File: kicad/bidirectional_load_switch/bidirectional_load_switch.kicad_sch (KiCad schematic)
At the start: 28 parts, among them J101 1017503, J102 Conn_01x09_Socket, J103 Conn_01x02_Socket, J104 Conn_01x02_Socket, J105 Conn_01x02_Socket, J106 Conn_01x02_Socket, J107 AVR-ISP-6, SW101 PTS526 SK15 SMTR2 LFS, U101 TMCS1101A3BQDR, U102 TLV75733PDBVR, U104 ATTINY85-20SU

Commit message: almost
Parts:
- added D101: CUS10S30_H3F, diode_CUS10S30_H3F:USC_TOS, symbol diode_CUS10S30_H3F:CUS10S30_H3F
- U102: footprint DBV0005A_N -> ldo_TLV75733PDBVR:DBV0005A_L
- renumbered C105 to C101, C106 to C102, C101 to C103, C107 to C104, C108 to C105, C104 to C106, C109 to C107, J103 to J102, J102 to J103, U104 to U103
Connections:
- net 3V3: now also D101.2
- net 5V: now also D101.1
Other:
- note added: "Power flags for DRC/ERC"
- moved on the sheet: C101, C102, C104, C105, J102, U102

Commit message: needs review
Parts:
- R101: value 10k -> 150
- SW101: footprint switch_switch_PTS526_SK15_SMTR2_LFS:SMT_FS -> switch_PTS526_SK15_SMTR2_LFS:SMT_FS
- U101: value TMCS1101A3BQDR -> TMCS1101A3BQDRQ1
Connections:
- net AC_in: now also U101.1 (IN+), U101.2 (IN+); no longer U101.3 (IN-), U101.4 (IN-)
- net AC_post_sense: now also U101.3 (IN-), U101.4 (IN-); no longer U101.1 (IN+), U101.2 (IN+)

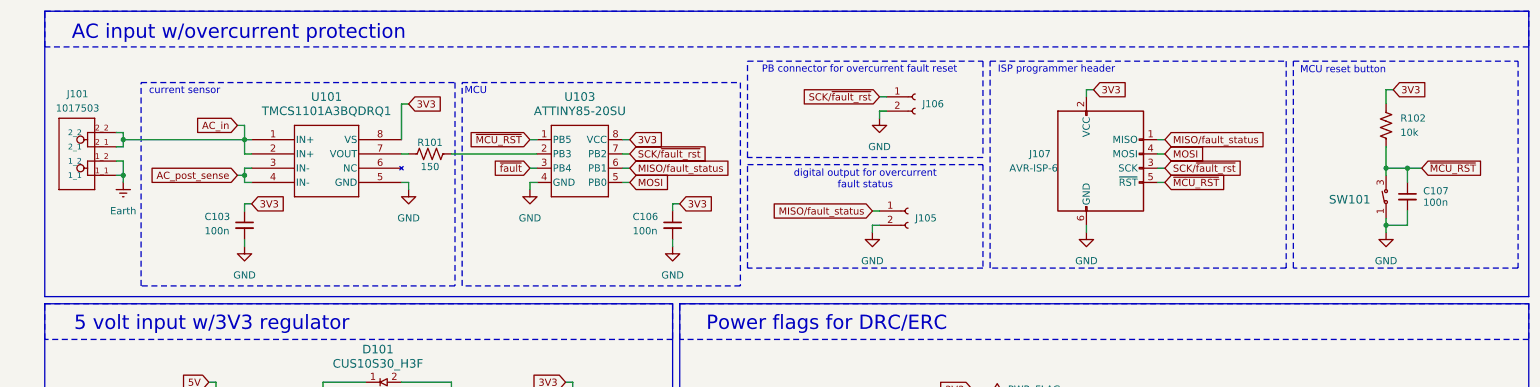
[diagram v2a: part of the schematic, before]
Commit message: added series diode for ISP 3V3 rail
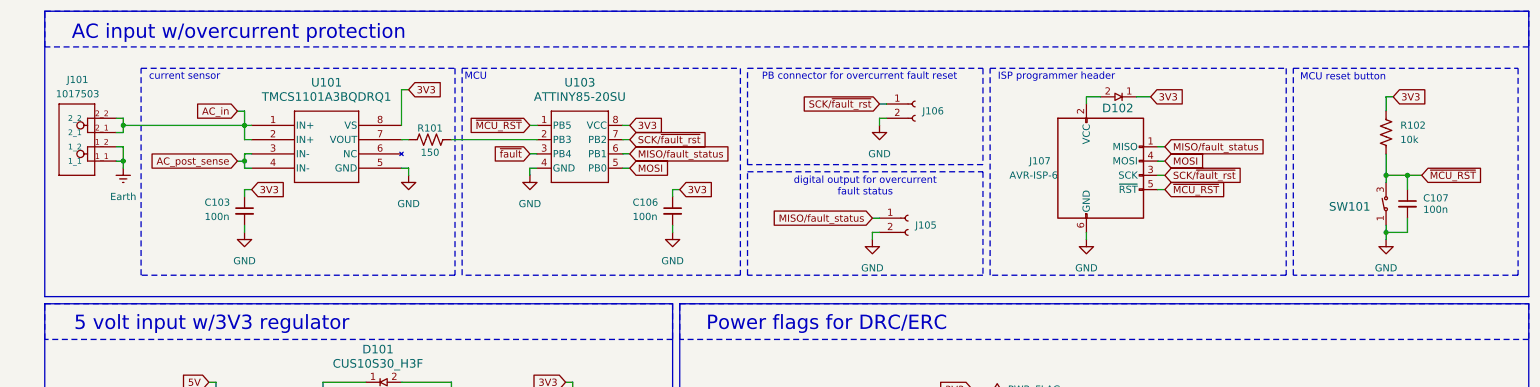
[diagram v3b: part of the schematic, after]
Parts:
- added D102: CUS10S30_H3F, diode_CUS10S30_H3F:USC_TOS, symbol diode_CUS10S30_H3F:CUS10S30_H3F
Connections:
- net 3V3: now also D102.1; no longer J107.2 (VCC)
- new net: D102.2, J107.2 (VCC)
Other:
- moved on the sheet: C103, C106, C107, J101, J105, J106, J107, R101, R102, SW101, U101, U103

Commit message: ready for order
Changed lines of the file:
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@@
 	(wire
 		(pts
-			(xy 110.49 92.71) (xy 110.49 93.98)
+			(xy 110.49 92.71) (xy 110.49 96.52)
 		)
 		(stroke
@@
 	(wire
 		(pts
-			(xy 46.99 92.71) (xy 46.99 93.98)
+			(xy 46.99 92.71) (xy 46.99 96.52)
 		)
 		(stroke
@@
 	(wire
 		(pts
-			(xy 128.27 54.61) (xy 128.27 55.88)
+			(xy 128.27 54.61) (xy 128.27 57.15)
 		)
 		(stroke
@@
 	(wire
 		(pts
-			(xy 52.07 54.61) (xy 52.07 55.88)
+			(xy 52.07 54.61) (xy 52.07 57.15)
 		)
 		(stroke
@@
 	(wire
 		(pts
-			(xy 25.4 92.71) (xy 25.4 90.17)
+			(xy 25.4 96.52) (xy 25.4 90.17)
 		)
 		(stroke
@@
 	(symbol
 		(lib_id "power:GND")
-		(at 128.27 55.88 0)
+		(at 128.27 57.15 0)
 		(unit 1)
 		(exclude_from_sim no)
@@
 		(fields_autoplaced yes)
 		(property "Reference" "#PWR0111"
-			(at 128.27 62.23 0)
+			(at 128.27 63.5 0)
 			(effects
 				(font
@@
 		)
 		(property "Value" "GND"
-			(at 128.27 60.96 0)
+			(at 128.27 62.23 0)
 			(effects
 				(font
@@
 		)
 		(property "Footprint" ""
-			(at 128.27 55.88 0)
+			(at 128.27 57.15 0)
 			(effects
 				(font
@@
 		)
 		(property "Datasheet" ""
-			(at 128.27 55.88 0)
+			(at 128.27 57.15 0)
 			(effects
 				(font
@@
 		)
 		(property "Description" "Power symbol creates a global label with name \"GND\" , ground"
-			(at 128.27 55.88 0)
+			(at 128.27 57.15 0)
 			(effects
 				(font
@@
 	(symbol
 		(lib_id "power:GND")
-		(at 25.4 92.71 0)
+		(at 25.4 96.52 0)
 		(unit 1)
 		(exclude_from_sim no)
@@
 		(fields_autoplaced yes)
 		(property "Reference" "#PWR0101"
-			(at 25.4 99.06 0)
+			(at 25.4 102.87 0)
 			(effects
 				(font
@@
 		)
 		(property "Value" "GND"
-			(at 25.4 97.79 0)
+			(at 25.4 101.6 0)
 			(effects
 				(font
@@
 		)
 		(property "Footprint" ""
-			(at 25.4 92.71 0)
+			(at 25.4 96.52 0)
 			(effects
 				(font
@@
 		)
 		(property "Datasheet" ""
-			(at 25.4 92.71 0)
+			(at 25.4 96.52 0)
 			(effects
 				(font
@@
 		)
 		(property "Description" "Power symbol creates a global label with name \"GND\" , ground"
-			(at 25.4 92.71 0)
+			(at 25.4 96.52 0)
 			(effects
 				(font
@@
 	(symbol
 		(lib_id "power:GND")
-		(at 52.07 55.88 0)
+		(at 52.07 57.15 0)
 		(unit 1)
 		(exclude_from_sim no)
@@
 		(fields_autoplaced yes)
 		(property "Reference" "#PWR0105"
-			(at 52.07 62.23 0)
+			(at 52.07 63.5 0)
 			(effects
 				(font
@@
 		)
 		(property "Value" "GND"
-			(at 52.07 60.96 0)
+			(at 52.07 62.23 0)
 			(effects
 				(font
@@
 		)
 		(property "Footprint" ""
-			(at 52.07 55.88 0)
+			(at 52.07 57.15 0)
 			(effects
 				(font
@@
 		)
 		(property "Datasheet" ""
-			(at 52.07 55.88 0)
+			(at 52.07 57.15 0)
 			(effects
 				(font
@@
 		)
 		(property "Description" "Power symbol creates a global label with name \"GND\" , ground"
-			(at 52.07 55.88 0)
+			(at 52.07 57.15 0)
 			(effects
 				(font
@@
 	(symbol
 		(lib_id "power:GND")
-		(at 110.49 93.98 0)
+		(at 110.49 96.52 0)
 		(unit 1)
 		(exclude_from_sim no)
@@
 		(fields_autoplaced yes)
 		(property "Reference" "#PWR0110"
-			(at 110.49 100.33 0)
+			(at 110.49 102.87 0)
 			(effects
 				(font
@@
 		)
 		(property "Value" "GND"
-			(at 110.49 99.06 0)
+			(at 110.49 101.6 0)
 			(effects
 				(font
@@
 		)
 		(property "Footprint" ""
-			(at 110.49 93.98 0)
+			(at 110.49 96.52 0)
 			(effects
 				(font
@@
 		)
 		(property "Datasheet" ""
-			(at 110.49 93.98 0)
+			(at 110.49 96.52 0)
 			(effects
 				(font
@@
 		)
 		(property "Description" "Power symbol creates a global label with name \"GND\" , ground"
-			(at 110.49 93.98 0)
+			(at 110.49 96.52 0)
 			(effects
 				(font
@@
 	(symbol
 		(lib_id "power:GND")
-		(at 46.99 93.98 0)
+		(at 46.99 96.52 0)
 		(unit 1)
 		(exclude_from_sim no)
@@
 		(fields_autoplaced yes)
 		(property "Reference" "#PWR0104"
-			(at 46.99 100.33 0)
+			(at 46.99 102.87 0)
 			(effects
 				(font
@@
 		)
 		(property "Value" "GND"
-			(at 46.99 99.06 0)
+			(at 46.99 101.6 0)
 			(effects
 				(font
@@
 		)
 		(property "Footprint" ""
-			(at 46.99 93.98 0)
+			(at 46.99 96.52 0)
 			(effects
 				(font
@@
 		)
 		(property "Datasheet" ""
-			(at 46.99 93.98 0)
+			(at 46.99 96.52 0)
 			(effects
 				(font
@@
 		)
 		(property "Description" "Power symbol creates a global label with name \"GND\" , ground"
-			(at 46.99 93.98 0)
+			(at 46.99 96.52 0)
 			(effects
 				(font

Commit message: updated gerbers
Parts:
- D101, D102: value CUS10S30_H3F -> ~; MPN (none) -> CUS10S30_H3F
- J101: value 1017503 -> ~; MPN (none) -> 1017503
- SW101: value PTS526 SK15 SMTR2 LFS -> ~; MPN (none) -> PTS526 SK15 SMTR2 LFS
- U101: value TMCS1101A3BQDRQ1 -> ~; MPN (none) -> TMCS1101A3BQDRQ1
- U102: value TLV75733PDBVR -> ~; MPN (none) -> TLV75733PDBVR
- U103: value ATTINY85-20SU -> ~; MPN (none) -> ATTINY85-20SU
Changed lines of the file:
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@@
 			)
 		)
-		(property "Value" "CUS10S30_H3F"
+		(property "Value" "~"
 			(at 217.932 32.258 0)
 			(effects
@@
 			)
 		)
+		(property "MPN" "CUS10S30_H3F"
+			(at 218.186 34.036 0)
+			(effects
+				(font
+					(size 1.27 1.27)
+				)
+			)
+		)
 		(pin "1"
 		)
@@
 			)
 		)
-		(property "Value" "TLV75733PDBVR"
+		(property "Value" "~"
 			(at 76.708 100.076 0)
 			(effects
@@
 					(size 1.524 1.524)
 				)
+				(hide yes)
 			)
 		)
@@
 			)
 		)
+		(property "MPN" "TLV75733PDBVR"
+			(at 76.708 99.822 0)
+			(effects
+				(font
+					(size 1.27 1.27)
+				)
+			)
+		)
 		(pin "2"
 		)
@@
 			)
 		)
-		(property "Value" "CUS10S30_H3F"
+		(property "Value" "~"
 			(at 75.819 79.248 0)
 			(effects
@@
 					(size 1.524 1.524)
 				)
+				(hide yes)
 			)
 		)
@@
 			)
 		)
+		(property "MPN" "CUS10S30_H3F"
+			(at 80.01 78.994 0)
+			(effects
+				(font
+					(size 1.27 1.27)
+				)
+			)
+		)
 		(pin "1"
 		)
@@
 			)
 		)
-		(property "Value" "PTS526 SK15 SMTR2 LFS"
+		(property "Value" "~"
 			(at 233.172 55.372 0)
 			(effects
@@
 			)
 		)
+		(property "MPN" "PTS526 SK15 SMTR2 LFS"
+			(at 255.27 54.61 90)
+			(effects
+				(font
+					(size 1.27 1.27)
+				)
+				(hide yes)
+			)
+		)
 		(pin "2"
 		)
@@
 		(dnp no)
 		(property "Reference" "U101"
-			(at 66.675 29.21 0)
+			(at 66.548 30.226 0)
 			(effects
 				(font
@@
 			)
 		)
-		(property "Value" "TMCS1101A3BQDRQ1"
+		(property "Value" "~"
 			(at 66.675 31.75 0)
 			(effects
@@
 					(size 1.524 1.524)
 				)
+				(hide yes)
 			)
 		)
@@
 			)
 		)
+		(property "MPN" "TMCS1101A3BQDRQ1"
+			(at 66.548 32.766 0)
+			(effects
+				(font
+					(size 1.27 1.27)
+				)
+			)
+		)
 		(pin "6"
 		)
@@
 		(on_board yes)
 		(dnp no)
-		(fields_autoplaced yes)
 		(property "Reference" "U103"
 			(at 111.76 29.21 0)
@@
 			)
 		)
-		(property "Value" "ATTINY85-20SU"
+		(property "Value" "~"
 			(at 111.76 31.75 0)
 			(effects
@@
 					(size 1.524 1.524)
 				)
+				(hide yes)
 			)
 		)
@@
 			)
 		)
+		(property "MPN" "ATTINY85-20SU"
+			(at 111.76 32.258 0)
+			(effects
+				(font
+					(size 1.27 1.27)
+				)
+			)
+		)
 		(pin "7"
 		)
@@
 			)
 		)
-		(property "Value" "1017503"
+		(property "Value" "~"
 			(at 22.352 31.242 0)
 			(effects
@@
 					(size 1.27 1.27)
 				)
+				(hide yes)
 			)
 		)
@@
 			)
 		)
-		(property "Datasheet" ""
+		(property "Datasheet" "https://mm.digikey.com/Volume0/opasdata/d220001/medias/docus/896/1017503_Ds.pdf"
 			(at 21.59 40.64 0)
 			(effects
@@
 			)
 		)
+		(property "MPN" "1017503"
+			(at 22.352 31.242 0)
+			(effects
+				(font
+					(size 1.27 1.27)
+				)
+			)
+		)

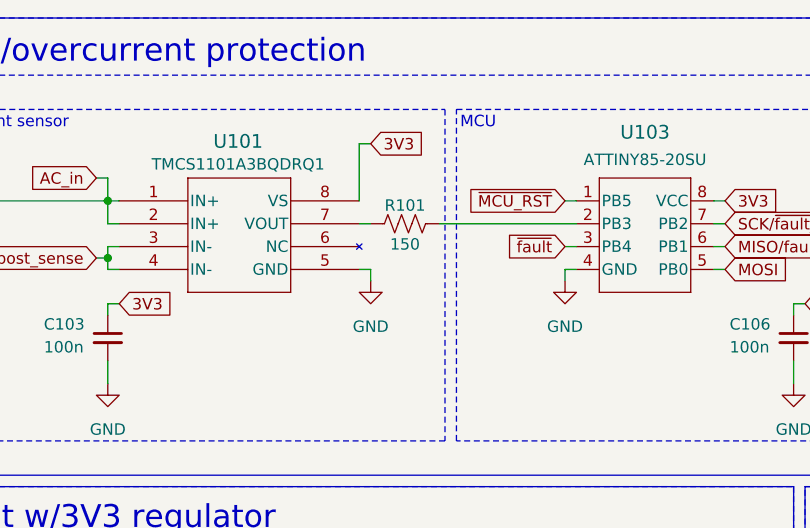
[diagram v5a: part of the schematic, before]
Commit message: removed redundant buffer
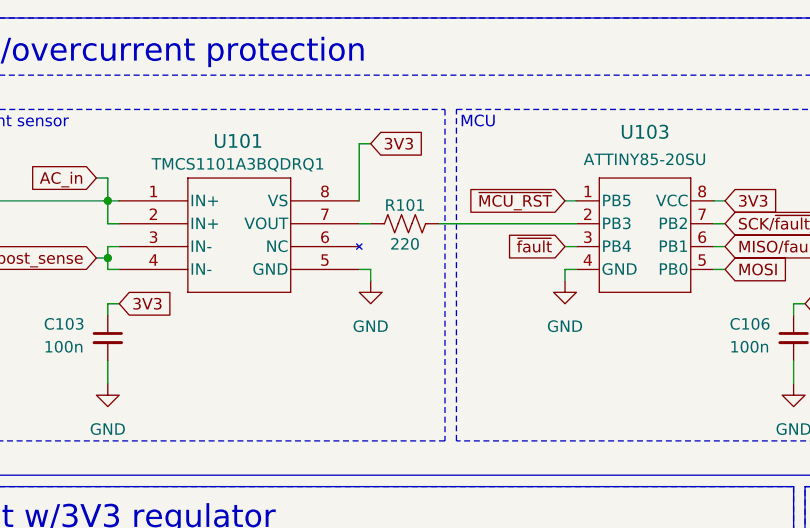
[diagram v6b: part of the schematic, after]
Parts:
- R101: value 150 -> 220
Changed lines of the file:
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@@
 			)
 		)
-		(property "Value" "150"
+		(property "Value" "220"
 			(at 85.09 41.656 90)
 			(effects

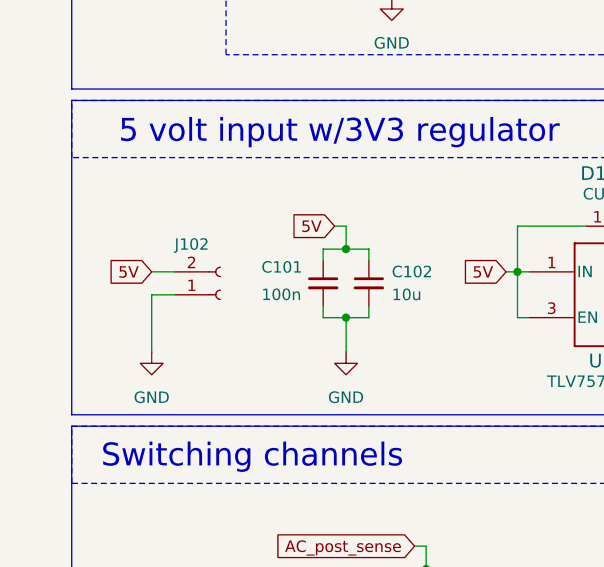
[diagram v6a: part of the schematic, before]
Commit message: updated connector polarity
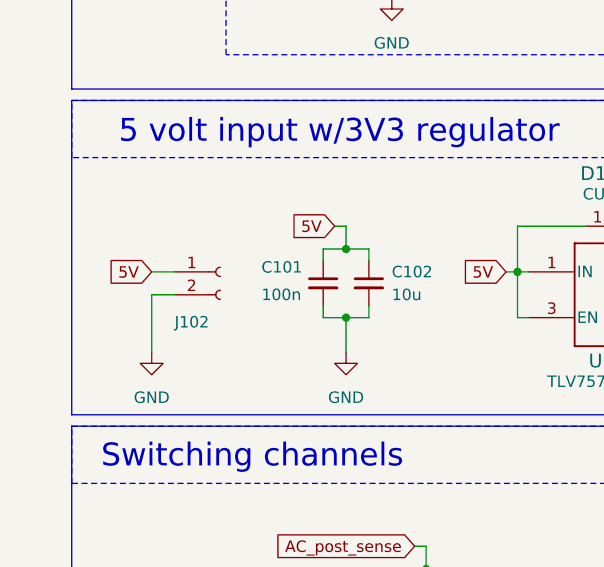
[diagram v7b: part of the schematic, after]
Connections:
- net 5V: now also J102.1 (Pin_1); no longer J102.2 (Pin_2)
- net GND: now also J102.2 (Pin_2); no longer J102.1 (Pin_1)
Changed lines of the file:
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@@
+	(wire
+		(pts
+			(xy 25.4 90.17) (xy 27.94 90.17)
+		)
+		(stroke
+			(width 0)
+			(type default)
+		)
+	)
 	(wire
 		(pts
@@
 		(pts
 			(xy 46.99 92.71) (xy 49.53 92.71)
-		)
-		(stroke
-			(width 0)
-			(type default)
-		)
-	)
-	(wire
-		(pts
-			(xy 25.4 90.17) (xy 27.94 90.17)
 		)
 		(stroke
@@
 	(symbol
 		(lib_id "Connector:Conn_01x02_Socket")
-		(at 33.02 90.17 0)
-		(mirror x)
+		(at 33.02 87.63 0)
 		(unit 1)
 		(exclude_from_sim no)
@@
 		(dnp no)
 		(property "Reference" "J102"
-			(at 27.94 84.582 0)
+			(at 27.94 93.218 0)
 			(effects
 				(font
@@
 		)
 		(property "Value" "Conn_01x02_Socket"
-			(at 34.29 87.6301 0)
+			(at 34.29 90.1699 0)
 			(effects
 				(font
@@
 		)
 		(property "Footprint" "Connector_PinHeader_2.54mm:PinHeader_1x02_P2.54mm_Vertical"
-			(at 33.02 90.17 0)
+			(at 33.02 87.63 0)
 			(effects
 				(font
@@
 		)
 		(property "Datasheet" "~"
-			(at 33.02 90.17 0)
+			(at 33.02 87.63 0)
 			(effects
 				(font
@@
 		)
 		(property "Description" "Generic connector, single row, 01x02, script generated"
-			(at 33.02 90.17 0)
-			(effects
-				(font
+			(at 33.02 87.63 0)
+			(effects
+				(font
